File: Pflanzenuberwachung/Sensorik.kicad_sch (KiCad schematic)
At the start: 4 parts, among them J10 Conn_01x03_Pin, J4 Conn_01x03_Pin, J5 Conn_01x04_Pin, Q2 BSS138

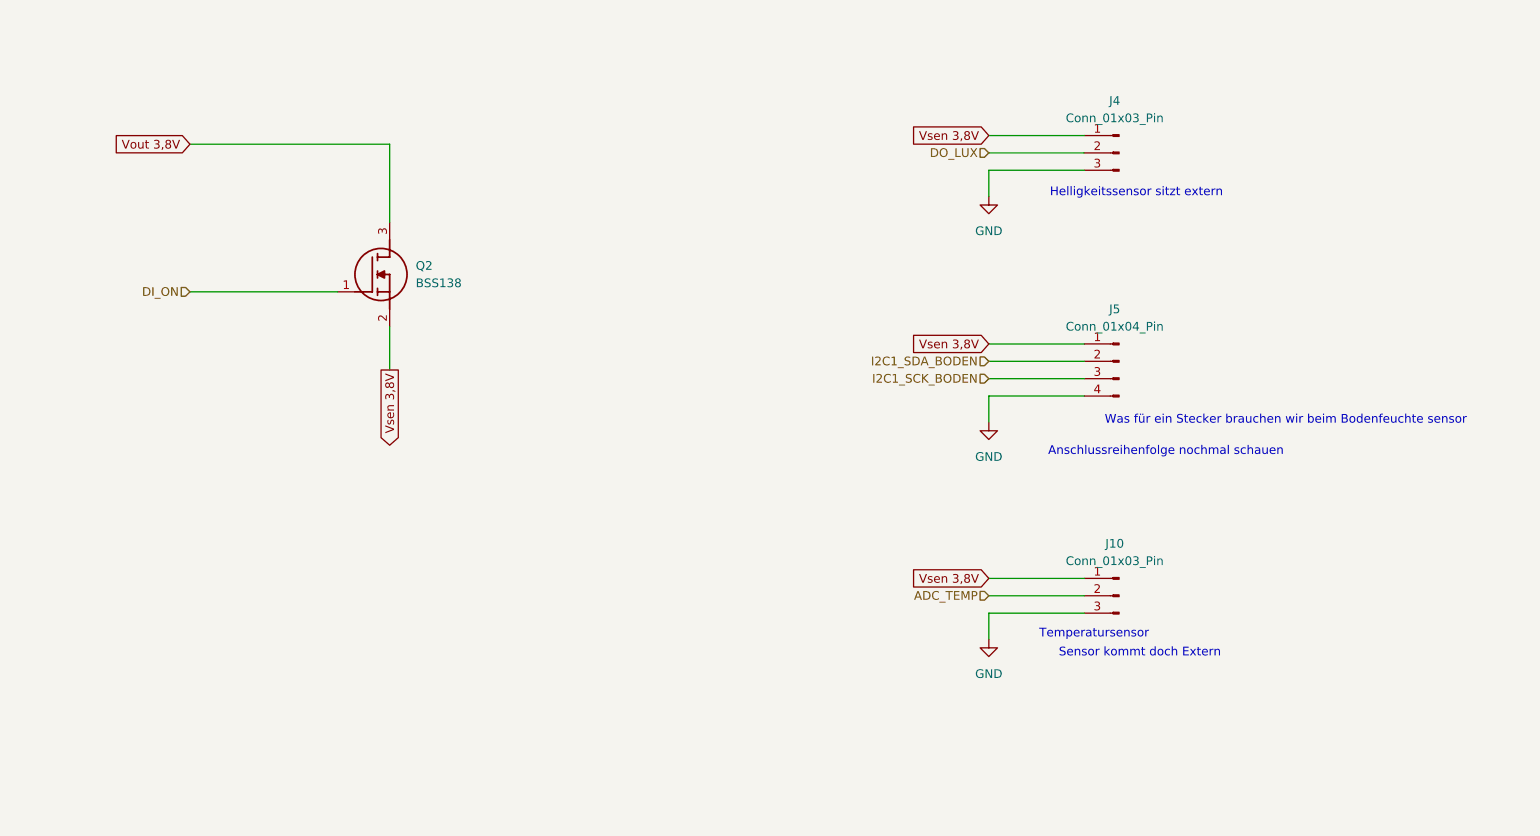
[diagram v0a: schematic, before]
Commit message: PCB Bord
PCB Design und kleiner nicht relevante änderungen
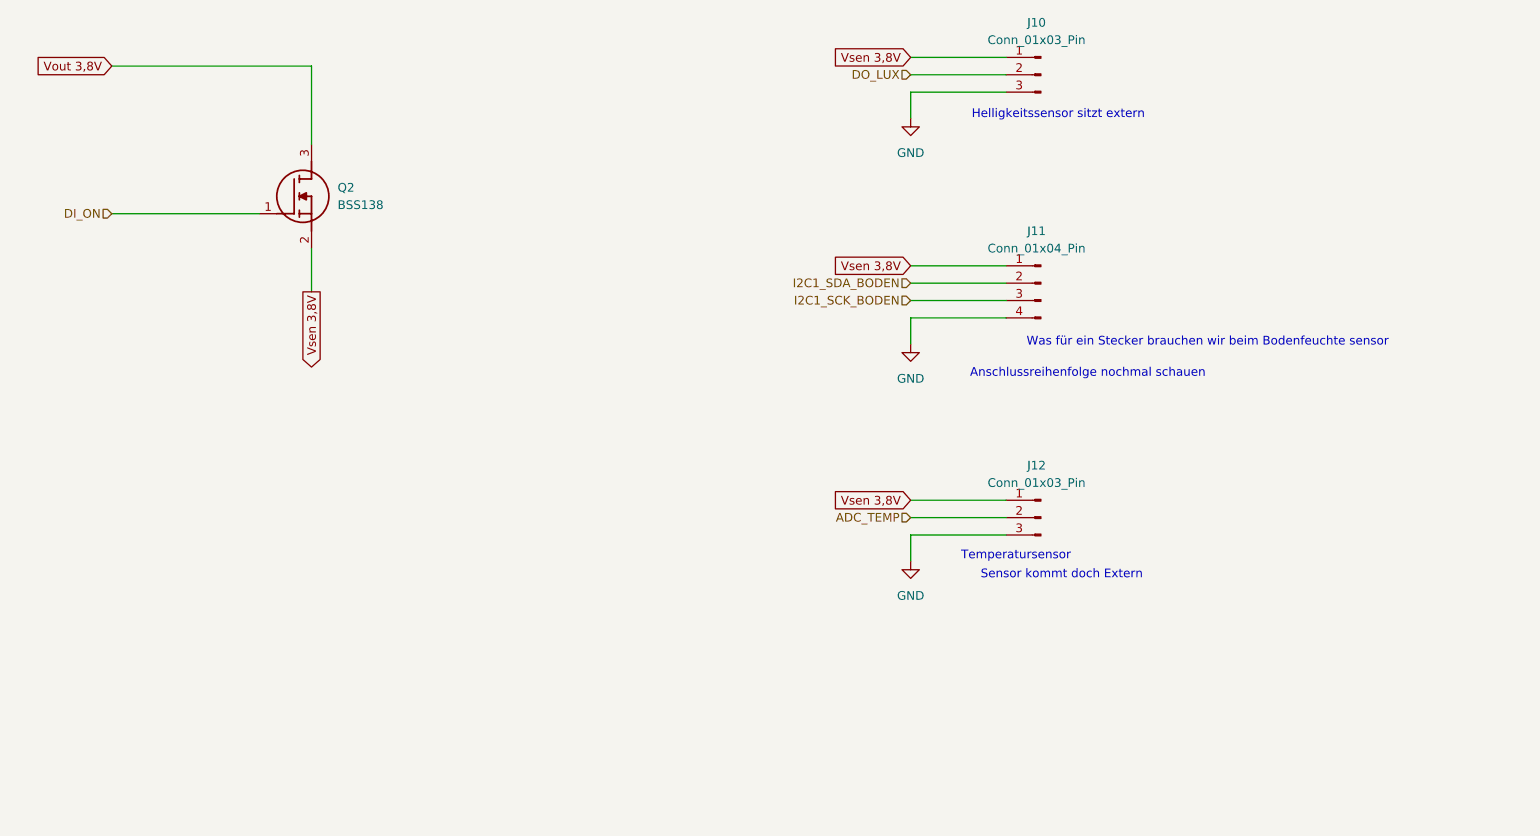
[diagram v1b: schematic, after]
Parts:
- removed J4: Conn_01x03_Pin, Connector_PinHeader_2.54mm:PinHeader_1x03_P2.54mm_Vertical, symbol Connector:Conn_01x03_Pin
- removed J5: Conn_01x04_Pin, Connector_PinHeader_2.54mm:PinHeader_1x04_P2.54mm_Vertical, symbol Connector:Conn_01x04_Pin
- added J11: Conn_01x04_Pin, Connector_PinHeader_2.54mm:PinHeader_1x04_P2.54mm_Vertical, symbol Connector:Conn_01x04_Pin
- added J12: Conn_01x03_Pin, Connector_PinHeader_2.54mm:PinHeader_1x03_P2.54mm_Vertical, symbol Connector:Conn_01x03_Pin
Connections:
- net ADC_TEMP: now also J12.2 (Pin_2); no longer J10.2 (Pin_2)
- net DO_LUX: now also J10.2 (Pin_2)
- net GND: now also J11.4 (Pin_4), J12.3 (Pin_3)
- net I2C1_SCK_BODEN: now also J11.3 (Pin_3)
- net I2C1_SDA_BODEN: now also J11.2 (Pin_2)
- net Vsen 3,8V: now also J11.1 (Pin_1), J12.1 (Pin_1)

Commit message: In Doku beschriebene Änderungen im Stromlaufplan eingefügt
Einfügen eins LDO für die Ausgangsspannung des BMS
Status LED für den Microprozessor
Ändern des MOSDED für die Sensoren von High Side zu Low Side
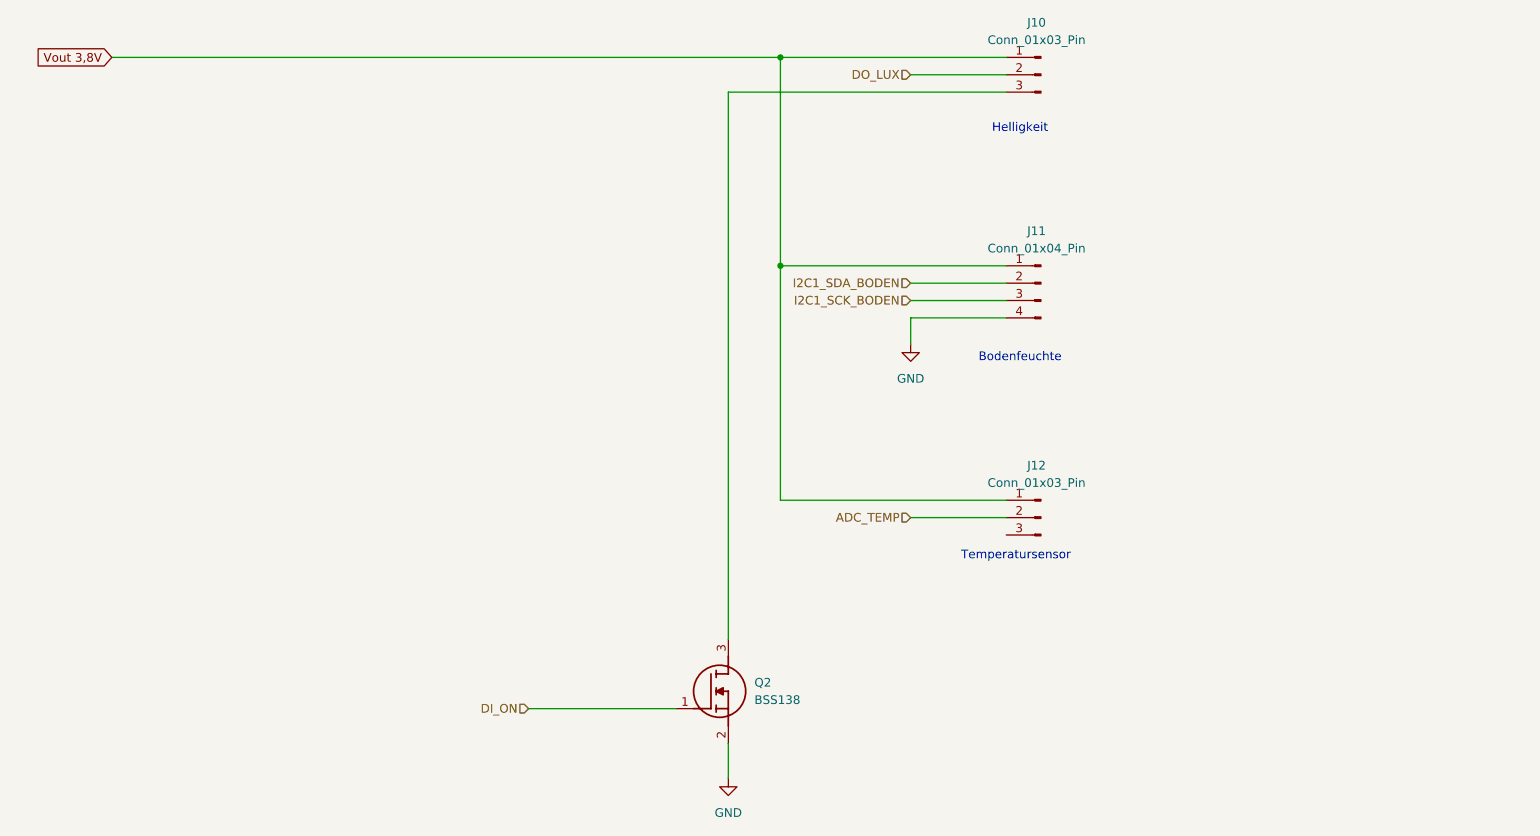
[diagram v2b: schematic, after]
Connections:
- net GND: now also Q2.2 (S); no longer J10.3 (Pin_3), J12.3 (Pin_3)
- net Vout 3,8V: now also J10.1 (Pin_1), J11.1 (Pin_1), J12.1 (Pin_1); no longer Q2.3 (D)
- removed net Vsen 3,8V: J10.1 (Pin_1), J11.1 (Pin_1), J12.1 (Pin_1), Q2.2 (S)
- new net: J10.3 (Pin_3), Q2.3 (D)
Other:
- note added: "Bodenfeuchte"
- note added: "Helligkeit"
- note removed: "Anschlussreihenfolge nochmal schauen"
- note removed: "Helligkeitssensor sitzt extern"
- note removed: "Sensor kommt doch Extern"
- note removed: "Was für ein Stecker brauchen wir beim Bodenfeuchte sensor"
- moved on the sheet: Q2
